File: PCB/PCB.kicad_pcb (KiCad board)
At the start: 2 copper layers, 0 parts

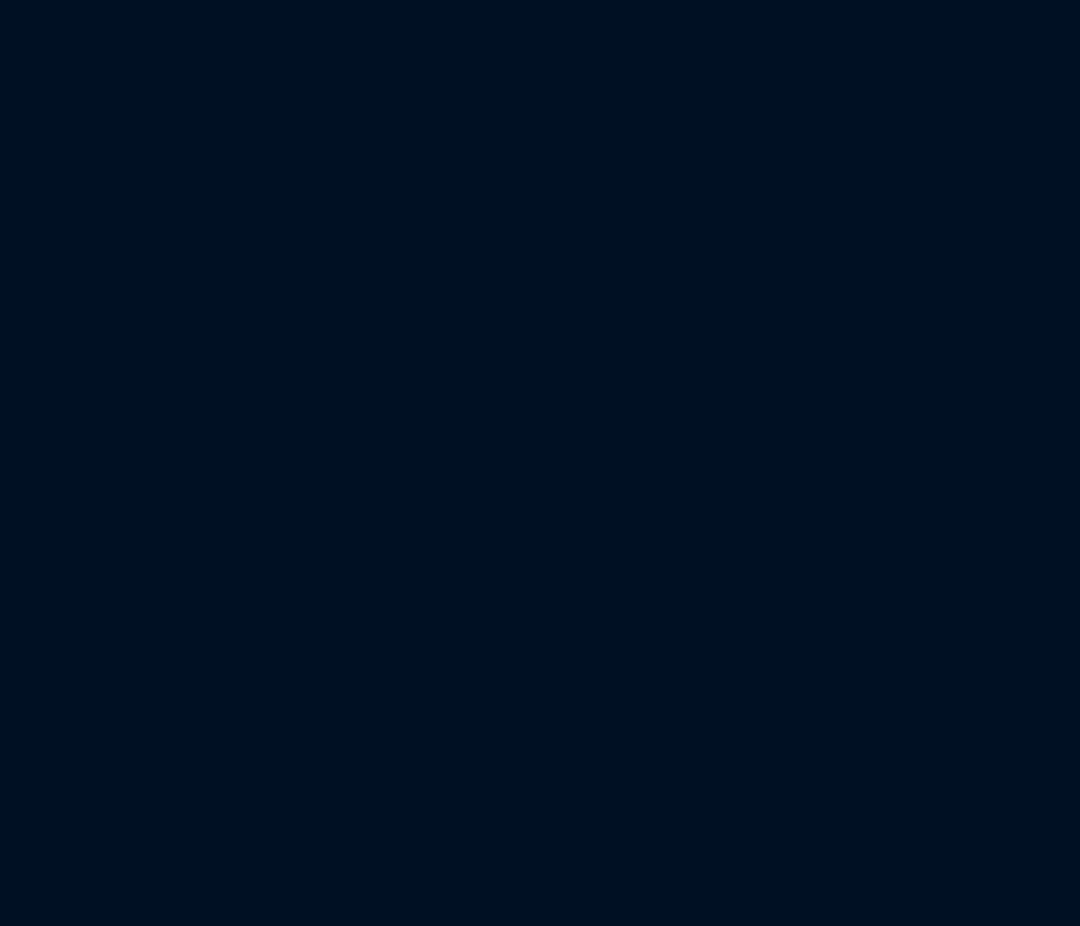
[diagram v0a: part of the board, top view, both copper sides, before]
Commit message: Confirm LCSC numbers
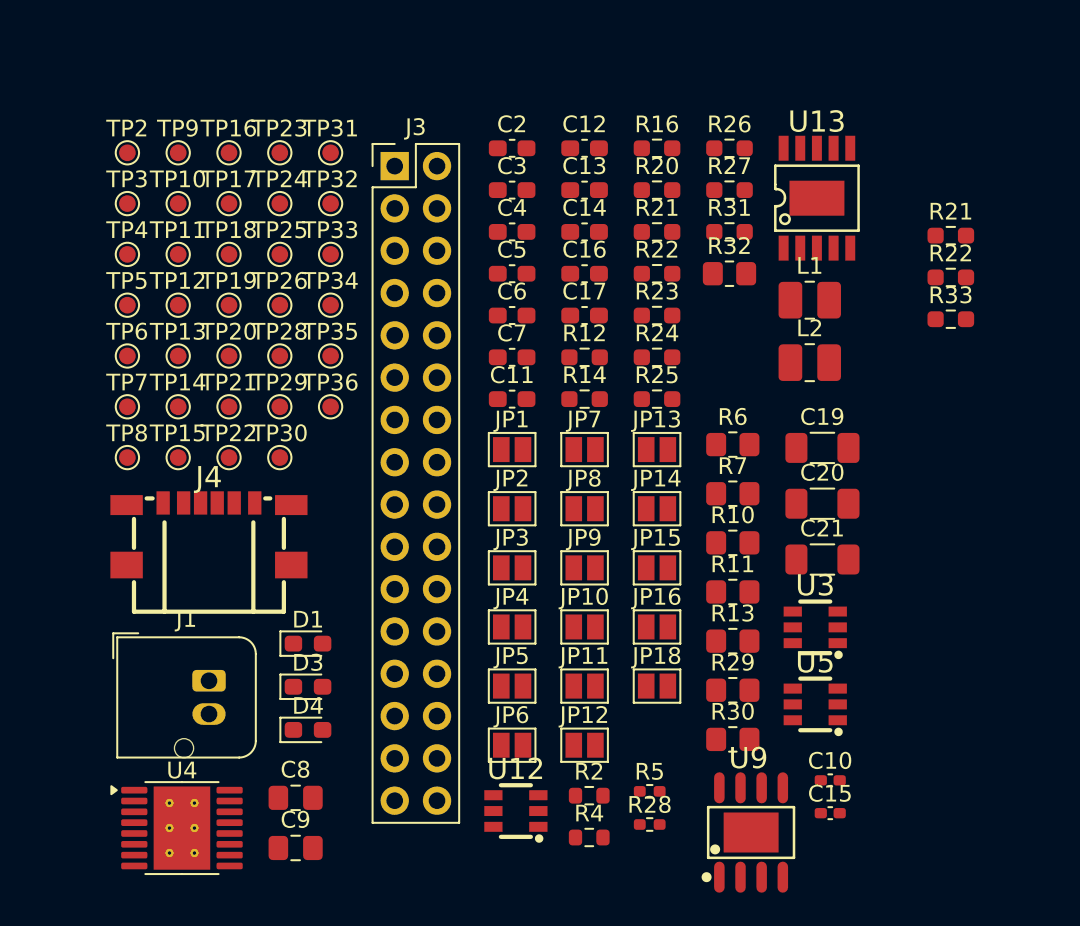
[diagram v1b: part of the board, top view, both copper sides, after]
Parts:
- added C10: 100n, Capacitor_SMD:C_0402_1005Metric_Pad0.74x0.62mm_HandSolder, F.Cu at (143.3, 109.7)
- added C11: 10u, Capacitor_SMD:C_0603_1608Metric_Pad1.08x0.95mm_HandSolder, F.Cu at (124.2, 86.8)
- added C12: 10u, Capacitor_SMD:C_0603_1608Metric_Pad1.08x0.95mm_HandSolder, F.Cu at (128.6, 71.7)
- added C13: 2.2u, Capacitor_SMD:C_0603_1608Metric_Pad1.08x0.95mm_HandSolder, F.Cu at (128.6, 74.2)
- added C14: 10u, Capacitor_SMD:C_0603_1608Metric_Pad1.08x0.95mm_HandSolder, F.Cu at (128.6, 76.8)
- added C15: 100n, Capacitor_SMD:C_0402_1005Metric_Pad0.74x0.62mm_HandSolder, F.Cu at (143.3, 111.7)
- added C16: 2.2u, Capacitor_SMD:C_0603_1608Metric_Pad1.08x0.95mm_HandSolder, F.Cu at (128.6, 79.3)
- added C17: 2.2u, Capacitor_SMD:C_0603_1608Metric_Pad1.08x0.95mm_HandSolder, F.Cu at (128.6, 81.8)
- added C19: 10u, Capacitor_SMD:C_1206_3216Metric_Pad1.33x1.80mm_HandSolder, F.Cu at (142.9, 89.7)
- added C2: 2.2u, Capacitor_SMD:C_0603_1608Metric_Pad1.08x0.95mm_HandSolder, F.Cu at (124.2, 71.7)
- added C20: 10u, Capacitor_SMD:C_1206_3216Metric_Pad1.33x1.80mm_HandSolder, F.Cu at (142.9, 93.1)
- added C21: 1u, Capacitor_SMD:C_1206_3216Metric_Pad1.33x1.80mm_HandSolder, F.Cu at (142.9, 96.4)
- added C3: 10u, Capacitor_SMD:C_0603_1608Metric_Pad1.08x0.95mm_HandSolder, F.Cu at (124.2, 74.2)
- added C4: 0.6u, Capacitor_SMD:C_0603_1608Metric_Pad1.08x0.95mm_HandSolder, F.Cu at (124.2, 76.8)
- added C5: 0.1u, Capacitor_SMD:C_0603_1608Metric_Pad1.08x0.95mm_HandSolder, F.Cu at (124.2, 79.3)
- added C6: 10u, Capacitor_SMD:C_0603_1608Metric_Pad1.08x0.95mm_HandSolder, F.Cu at (124.2, 81.8)
- added C7: 10u, Capacitor_SMD:C_0603_1608Metric_Pad1.08x0.95mm_HandSolder, F.Cu at (124.2, 84.3)
- added C8: 47u, Capacitor_SMD:C_0805_2012Metric_Pad1.18x1.45mm_HandSolder, F.Cu at (111.2, 110.7)
- added C9: 47u, Capacitor_SMD:C_0805_2012Metric_Pad1.18x1.45mm_HandSolder, F.Cu at (111.2, 113.7)
- added D1: LED, LED_SMD:LED_0603_1608Metric_Pad1.05x0.95mm_HandSolder, F.Cu at (112.0, 101.5)
- added D3: Red, LED_SMD:LED_0603_1608Metric_Pad1.05x0.95mm_HandSolder, F.Cu at (112.0, 104.1)
- added D4: LED, LED_SMD:LED_0603_1608Metric_Pad1.05x0.95mm_HandSolder, F.Cu at (112.0, 106.7)
- added J1: Conn_01x02_Pin, Connector_JST:JST_JWPF_B02B-JWPF-SK-R_1x02_P2.00mm_Vertical, F.Cu at (106.0, 103.7)
- added J3: Conn_02x16_Odd_Even, Connector_PinHeader_2.54mm:PinHeader_2x16_P2.54mm_Vertical, F.Cu at (117.2, 72.8)
- added J4: USB_C_Receptacle_PowerOnly_6P, Nhlamolo.:USB-C-SMD_TYPE-602-T3, F.Cu at (106.0, 94.9)
- added JP1: Jumper_2_Small_Open, Jumper:SolderJumper-2_P1.3mm_Open_Pad1.0x1.5mm, F.Cu at (124.2, 89.8)
- added JP10: Jumper_2_Small_Open, Jumper:SolderJumper-2_P1.3mm_Open_Pad1.0x1.5mm, F.Cu at (128.6, 100.5)
- added JP11: Jumper_2_Small_Open, Jumper:SolderJumper-2_P1.3mm_Open_Pad1.0x1.5mm, F.Cu at (128.6, 104.0)
- added JP12: Jumper_2_Small_Open, Jumper:SolderJumper-2_P1.3mm_Open_Pad1.0x1.5mm, F.Cu at (128.6, 107.6)
- added JP13: Jumper_2_Small_Open, Jumper:SolderJumper-2_P1.3mm_Open_Pad1.0x1.5mm, F.Cu at (132.9, 89.8)
- added JP14: Jumper_2_Small_Open, Jumper:SolderJumper-2_P1.3mm_Open_Pad1.0x1.5mm, F.Cu at (132.9, 93.4)
- added JP15: Jumper_2_Small_Open, Jumper:SolderJumper-2_P1.3mm_Open_Pad1.0x1.5mm, F.Cu at (132.9, 96.9)
- added JP16: Jumper_2_Small_Open, Jumper:SolderJumper-2_P1.3mm_Open_Pad1.0x1.5mm, F.Cu at (132.9, 100.5)
- added JP18: Jumper_2_Small_Open, Jumper:SolderJumper-2_P1.3mm_Open_Pad1.0x1.5mm, F.Cu at (132.9, 104.0)
- added JP2: Jumper_2_Small_Open, Jumper:SolderJumper-2_P1.3mm_Open_Pad1.0x1.5mm, F.Cu at (124.2, 93.4)
- added JP3: Jumper_2_Small_Open, Jumper:SolderJumper-2_P1.3mm_Open_Pad1.0x1.5mm, F.Cu at (124.2, 96.9)
- added JP4: Jumper_2_Small_Open, Jumper:SolderJumper-2_P1.3mm_Open_Pad1.0x1.5mm, F.Cu at (124.2, 100.5)
- added JP5: Jumper_2_Small_Open, Jumper:SolderJumper-2_P1.3mm_Open_Pad1.0x1.5mm, F.Cu at (124.2, 104.0)
- added JP6: Jumper_2_Small_Open, Jumper:SolderJumper-2_P1.3mm_Open_Pad1.0x1.5mm, F.Cu at (124.2, 107.6)
- added JP7: Jumper_2_Small_Open, Jumper:SolderJumper-2_P1.3mm_Open_Pad1.0x1.5mm, F.Cu at (128.6, 89.8)
- added JP8: Jumper_2_Small_Open, Jumper:SolderJumper-2_P1.3mm_Open_Pad1.0x1.5mm, F.Cu at (128.6, 93.4)
- added JP9: Jumper_2_Small_Open, Jumper:SolderJumper-2_P1.3mm_Open_Pad1.0x1.5mm, F.Cu at (128.6, 96.9)
- added L1: 2.2u, Inductor_SMD:L_1008_2520Metric_Pad1.43x2.20mm_HandSolder, F.Cu at (142.1, 80.9)
- added L2: 2.2u, Inductor_SMD:L_1008_2520Metric_Pad1.43x2.20mm_HandSolder, F.Cu at (142.1, 84.6)
- added R10: 200, Resistor_SMD:R_0805_2012Metric_Pad1.20x1.40mm_HandSolder, F.Cu at (137.5, 95.4)
- added R11: 200, Resistor_SMD:R_0805_2012Metric_Pad1.20x1.40mm_HandSolder, F.Cu at (137.5, 98.4)
- added R12: 0, Resistor_SMD:R_0603_1608Metric_Pad0.98x0.95mm_HandSolder, F.Cu at (128.6, 84.3)
- added R13: 5k6, Resistor_SMD:R_0805_2012Metric_Pad1.20x1.40mm_HandSolder, F.Cu at (137.5, 101.3)
- added R14: 1k, Resistor_SMD:R_0603_1608Metric_Pad0.98x0.95mm_HandSolder, F.Cu at (128.6, 86.8)
- added R16: 1k, Resistor_SMD:R_0603_1608Metric_Pad0.98x0.95mm_HandSolder, F.Cu at (132.9, 71.7)
- added R2: 1.8k, Resistor_SMD:R_0603_1608Metric, F.Cu at (128.9, 110.6)
- added R20: 0.2, Resistor_SMD:R_0603_1608Metric_Pad0.98x0.95mm_HandSolder, F.Cu at (132.9, 74.2)
- added R21: 200m, Resistor_SMD:R_0603_1608Metric_Pad0.98x0.95mm_HandSolder, F.Cu at (132.9, 76.8)
- added R21: 0.2, Resistor_SMD:R_0603_1608Metric_Pad0.98x0.95mm_HandSolder, F.Cu at (150.6, 77.0)
- added R22: 0.2, Resistor_SMD:R_0603_1608Metric_Pad0.98x0.95mm_HandSolder, F.Cu at (150.6, 79.5)
- added R22: 200m, Resistor_SMD:R_0603_1608Metric_Pad0.98x0.95mm_HandSolder, F.Cu at (132.9, 79.3)
- added R23: 200m, Resistor_SMD:R_0603_1608Metric_Pad0.98x0.95mm_HandSolder, F.Cu at (132.9, 81.8)
- added R24: 4.7k, Resistor_SMD:R_0603_1608Metric_Pad0.98x0.95mm_HandSolder, F.Cu at (132.9, 84.3)
- added R25: 1k8, Resistor_SMD:R_0603_1608Metric_Pad0.98x0.95mm_HandSolder, F.Cu at (132.9, 86.8)
- added R26: 0, Resistor_SMD:R_0603_1608Metric_Pad0.98x0.95mm_HandSolder, F.Cu at (137.3, 71.7)
- added R27: 4.7k, Resistor_SMD:R_0603_1608Metric_Pad0.98x0.95mm_HandSolder, F.Cu at (137.3, 74.2)
- added R28: 1k, Resistor_SMD:R_0402_1005Metric_Pad0.72x0.64mm_HandSolder, F.Cu at (132.5, 112.3)
- added R29: 6k8, Resistor_SMD:R_0805_2012Metric_Pad1.20x1.40mm_HandSolder, F.Cu at (137.5, 104.3)
- added R30: 10k, Resistor_SMD:R_0805_2012Metric_Pad1.20x1.40mm_HandSolder, F.Cu at (137.5, 107.2)
- added R31: 10k, Resistor_SMD:R_0603_1608Metric_Pad0.98x0.95mm_HandSolder, F.Cu at (137.3, 76.8)
- added R32: 10k, Resistor_SMD:R_0805_2012Metric_Pad1.20x1.40mm_HandSolder, F.Cu at (137.3, 79.3)
- added R33: 0.2, Resistor_SMD:R_0603_1608Metric_Pad0.98x0.95mm_HandSolder, F.Cu at (150.6, 82.0)
- added R4: 1.8k, Resistor_SMD:R_0603_1608Metric, F.Cu at (128.9, 113.1)
- added R5: 1k, Resistor_SMD:R_0402_1005Metric_Pad0.72x0.64mm_HandSolder, F.Cu at (132.5, 110.3)
- added R6: 10k, Resistor_SMD:R_0805_2012Metric_Pad1.20x1.40mm_HandSolder, F.Cu at (137.5, 89.5)
- added R7: 8.2k, Resistor_SMD:R_0805_2012Metric_Pad1.20x1.40mm_HandSolder, F.Cu at (137.5, 92.5)
- added TP10: TestPoint, TestPoint:TestPoint_Pad_D1.0mm, F.Cu at (104.2, 75.1)
- added TP11: TestPoint, TestPoint:TestPoint_Pad_D1.0mm, F.Cu at (104.2, 78.1)
- added TP12: TestPoint, TestPoint:TestPoint_Pad_D1.0mm, F.Cu at (104.2, 81.2)
- added TP13: TestPoint, TestPoint:TestPoint_Pad_D1.0mm, F.Cu at (104.2, 84.2)
- added TP14: TestPoint, TestPoint:TestPoint_Pad_D1.0mm, F.Cu at (104.2, 87.3)
- added TP15: TestPoint, TestPoint:TestPoint_Pad_D1.0mm, F.Cu at (104.2, 90.3)
- added TP16: TestPoint, TestPoint:TestPoint_Pad_D1.0mm, F.Cu at (107.2, 72.0)
- added TP17: TestPoint, TestPoint:TestPoint_Pad_D1.0mm, F.Cu at (107.2, 75.1)
- added TP18: TestPoint, TestPoint:TestPoint_Pad_D1.0mm, F.Cu at (107.2, 78.1)
- added TP19: TestPoint, TestPoint:TestPoint_Pad_D1.0mm, F.Cu at (107.2, 81.2)
- added TP2: TestPoint, TestPoint:TestPoint_Pad_D1.0mm, F.Cu at (101.1, 72.0)
- added TP20: TestPoint, TestPoint:TestPoint_Pad_D1.0mm, F.Cu at (107.2, 84.2)
- added TP21: TestPoint, TestPoint:TestPoint_Pad_D1.0mm, F.Cu at (107.2, 87.3)
- added TP22: TestPoint, TestPoint:TestPoint_Pad_D1.0mm, F.Cu at (107.2, 90.3)
- added TP23: TestPoint, TestPoint:TestPoint_Pad_D1.0mm, F.Cu at (110.3, 72.0)
- added TP24: TestPoint, TestPoint:TestPoint_Pad_D1.0mm, F.Cu at (110.3, 75.1)
- added TP25: TestPoint, TestPoint:TestPoint_Pad_D1.0mm, F.Cu at (110.3, 78.1)
- added TP26: TestPoint, TestPoint:TestPoint_Pad_D1.0mm, F.Cu at (110.3, 81.2)
- added TP28: TestPoint, TestPoint:TestPoint_Pad_D1.0mm, F.Cu at (110.3, 84.2)
- added TP29: TestPoint, TestPoint:TestPoint_Pad_D1.0mm, F.Cu at (110.3, 87.3)
- added TP3: TestPoint, TestPoint:TestPoint_Pad_D1.0mm, F.Cu at (101.1, 75.1)
- added TP30: TestPoint, TestPoint:TestPoint_Pad_D1.0mm, F.Cu at (110.3, 90.3)
- added TP31: TestPoint, TestPoint:TestPoint_Pad_D1.0mm, F.Cu at (113.3, 72.0)
- added TP32: TestPoint, TestPoint:TestPoint_Pad_D1.0mm, F.Cu at (113.3, 75.1)
- added TP33: TestPoint, TestPoint:TestPoint_Pad_D1.0mm, F.Cu at (113.3, 78.1)
- added TP34: TestPoint, TestPoint:TestPoint_Pad_D1.0mm, F.Cu at (113.3, 81.2)
- added TP35: TestPoint, TestPoint:TestPoint_Pad_D1.0mm, F.Cu at (113.3, 84.2)
- added TP36: TestPoint, TestPoint:TestPoint_Pad_D1.0mm, F.Cu at (113.3, 87.3)
- added TP4: TestPoint, TestPoint:TestPoint_Pad_D1.0mm, F.Cu at (101.1, 78.1)
- added TP5: TestPoint, TestPoint:TestPoint_Pad_D1.0mm, F.Cu at (101.1, 81.2)
- added TP6: TestPoint, TestPoint:TestPoint_Pad_D1.0mm, F.Cu at (101.1, 84.2)
- added TP7: TestPoint, TestPoint:TestPoint_Pad_D1.0mm, F.Cu at (101.1, 87.3)
- added TP8: TestPoint, TestPoint:TestPoint_Pad_D1.0mm, F.Cu at (101.1, 90.3)
- added TP9: TestPoint, TestPoint:TestPoint_Pad_D1.0mm, F.Cu at (104.2, 72.0)
- added U12: TS5A3159ADBVR, Nhlamolo.:SOT-23-6_L2.9-W1.6-P0.95-LS2.8-BR, F.Cu at (124.5, 111.5)
- added U13: CH224K, Nhlamolo.:ESSOP-10_L4.9-W3.9-P1.0-LS6.0-TL-EP, F.Cu at (142.5, 74.7)
- added U3: TPS22917DBV, Nhlamolo.:SOT-23-6_L2.9-W1.6-P0.95-LS2.8-BR, F.Cu at (142.4, 100.5)
- added U4: DRV8833PWP, Package_SO:HTSSOP-16-1EP_4.4x5mm_P0.65mm_EP3.4x5mm_Mask2.46x2.31mm_ThermalVias, F.Cu at (104.4, 112.6)
- added U5: TPS22917DBV, Nhlamolo.:SOT-23-6_L2.9-W1.6-P0.95-LS2.8-BR, F.Cu at (142.4, 105.1)
- added U9: TP4056-42-ESOP8, Nhlamolo.:ESOP-8_L4.9-W3.9-P1.27-LS6.0-BL-EP-1, F.Cu at (138.6, 112.8)

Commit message: Before PCB layout
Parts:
- removed C20: 10u, Capacitor_SMD:C_1206_3216Metric_Pad1.33x1.80mm_HandSolder
- removed JP12, JP13: Jumper_2_Small_Open, Jumper:SolderJumper-2_P1.3mm_Open_Pad1.0x1.5mm
- removed R20, R21, R22, R33: 0.2, Resistor_SMD:R_0603_1608Metric_Pad0.98x0.95mm_HandSolder
- removed R21, R22, R23: 200m, Resistor_SMD:R_0603_1608Metric_Pad0.98x0.95mm_HandSolder
- removed R26: 0, Resistor_SMD:R_0603_1608Metric_Pad0.98x0.95mm_HandSolder
- removed TP15, TP16, TP17, TP18, TP28, TP29, TP31, TP5: TestPoint, TestPoint:TestPoint_Pad_D1.0mm
- removed U12: TS5A3159ADBVR, Nhlamolo.:SOT-23-6_L2.9-W1.6-P0.95-LS2.8-BR
- removed U13: CH224K, Nhlamolo.:ESSOP-10_L4.9-W3.9-P1.0-LS6.0-TL-EP
- removed U3, U5: TPS22917DBV, Nhlamolo.:SOT-23-6_L2.9-W1.6-P0.95-LS2.8-BR
- removed U9: TP4056-42-ESOP8, Nhlamolo.:ESOP-8_L4.9-W3.9-P1.27-LS6.0-BL-EP-1
- added C22: 10u, Capacitor_SMD:C_0603_1608Metric_Pad1.08x0.95mm_HandSolder, F.Cu at (272.2, 136.0)
- added JP17: Jumper_2_Small_Open, Jumper:SolderJumper-2_P1.3mm_Open_Pad1.0x1.5mm, F.Cu at (272.2, 83.3)
- added JP19: Jumper_2_Small_Open, Jumper:SolderJumper-2_P1.3mm_Open_Pad1.0x1.5mm, F.Cu at (272.2, 90.5)
- added JP21: Jumper_2_Small_Open, Jumper:SolderJumper-2_P1.3mm_Open_Pad1.0x1.5mm, F.Cu at (272.2, 94.0)
- added JP22: Jumper_2_Small_Open, Jumper:SolderJumper-2_P1.3mm_Open_Pad1.0x1.5mm, F.Cu at (272.2, 97.5)
- added JP23: Jumper_2_Small_Open, Jumper:SolderJumper-2_P1.3mm_Open_Pad1.0x1.5mm, F.Cu at (272.2, 101.1)
- added JP24: Jumper_2_Small_Open, Jumper:SolderJumper-2_P1.3mm_Open_Pad1.0x1.5mm, F.Cu at (272.2, 104.7)
- added R15: 0.22, Library:R2512, F.Cu at (247.3, 100.6)
- added R17: 0.22, Library:R2512, F.Cu at (247.3, 105.7)
- added R18: 0.22, Library:R2512, F.Cu at (247.3, 110.7)
- added R19: 0.22, Library:R2512, F.Cu at (247.3, 115.8)
- added R8: 0.22, Library:R2512, F.Cu at (247.3, 85.4)
- added R9: 0.22, Library:R2512, F.Cu at (247.3, 90.5)
- added SW1: SW_Nidec_CAS-120A1, Library:SW-TH_1MS1T1B1M1QES-5, F.Cu at (249.6, 138.7)
- added TP27: TestPoint, TestPoint:TestPoint_Pad_D1.0mm, F.Cu at (272.0, 114.0)
- added TP37: TestPoint, TestPoint:TestPoint_THTPad_D2.5mm_Drill1.2mm, F.Cu at (205.3, 107.4)
- added TP38: TestPoint, TestPoint:TestPoint_THTPad_D2.5mm_Drill1.2mm, F.Cu at (205.3, 112.0)
- added TP39: TestPoint, TestPoint:TestPoint_Pad_D1.0mm, F.Cu at (275.1, 117.1)
- added TP40: TestPoint, TestPoint:TestPoint_Pad_D1.0mm, F.Cu at (275.1, 120.2)
- added U1: DRV8833PWPR, Library:DRV8833PWPR, F.Cu at (212.5, 108.2)
- added U10: TPS63020, Library:TPS63020DSJR, F.Cu at (99.8, 178.8)
- added U11: TPS63020, Library:TPS63020DSJR, F.Cu at (159.5, 187.5)
- added U2: INA219AxDCN, Library:INA219AIDCNR, F.Cu at (210.0, 113.4)
- C10, C15: footprint Capacitor_SMD:C_0402_1005Metric_Pad0.74x0.62mm_HandSolder -> Capacitor_SMD:C_0603_1608Metric_Pad1.08x0.95mm_HandSolder
- C19, C21: footprint Capacitor_SMD:C_1206_3216Metric_Pad1.33x1.80mm_HandSolder -> Capacitor_SMD:C_0603_1608Metric_Pad1.08x0.95mm_HandSolder
- C4: value 0.6u -> 1u
- J4: footprint Nhlamolo.:USB-C-SMD_TYPE-602-T3 -> Connector_USB:USB_C_Receptacle_GCT_USB4110
- R12: value 0 -> 0.22; footprint Resistor_SMD:R_0603_1608Metric_Pad0.98x0.95mm_HandSolder -> Library:R2512
- R28, R5: footprint Resistor_SMD:R_0402_1005Metric_Pad0.72x0.64mm_HandSolder -> Resistor_SMD:R_0603_1608Metric_Pad0.98x0.95mm_HandSolder
- R31: footprint Resistor_SMD:R_0603_1608Metric_Pad0.98x0.95mm_HandSolder -> Resistor_SMD:R_0805_2012Metric_Pad1.20x1.40mm_HandSolder
- moved TP23 165.8 mm to (268.9, 120.2)
- moved TP24 165.8 mm to (268.9, 123.2)
- moved TP2 165.6 mm to (262.9, 108.0)
- moved TP3 165.6 mm to (262.9, 111.0)
- moved TP4 165.6 mm to (262.9, 114.0)
- moved TP10 165.6 mm to (265.9, 111.0)
- moved TP11 165.6 mm to (265.9, 114.0)
- moved TP12 165.6 mm to (265.9, 117.1)
- moved TP13 165.6 mm to (265.9, 120.2)
- moved TP14 165.6 mm to (265.9, 123.2)
- moved TP9 165.6 mm to (265.9, 108.0)
- moved TP6 165.0 mm to (262.9, 117.1)
- moved TP7 165.0 mm to (262.9, 120.2)
- moved TP8 165.0 mm to (262.9, 123.2)
- moved TP32 164.9 mm to (272.0, 120.2)
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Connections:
- C4 pad 1: Net-(U2-IN+) -> Battery
- C4 pad 2: Net-(U2-IN-) -> Load_Supply
- J1 pad 1: unconnected-(J1-Pin_1-Pad1) -> Net-(J1-Pin_1)
- J4 pad A9: /HV_Pin -> High_Voltage_(9V)
- J4 pad B9: /HV_Pin -> High_Voltage_(9V)
- JP16 pad 1: /5V_PG -> Load_Supply
- JP16 pad 2: 5V Out -> Net-(JP16-B)
- R12 pad 1: Battery -> GND
- R12 pad 2: Net-(U2-IN+) -> Net-(JP1-B)
- R28 pad 1: /HV_Pin -> High_Voltage_(9V)
- R31 pad 2: /5V_Out -> Net-(JP17-B)
- R6 pad 1: /HV-Pin -> High_Voltage_(9V)
- TP19 pad 1: Load_Supply -> /3V3_Out
- TP2 pad 1: Battery -> Net-(JP19-B)
- TP20 pad 1: Battery -> MOTOR3_A_OUT
- TP22 pad 1: I2C1_SDA -> MOTOR4_A_OUT
- TP23 pad 1: I2C1_SCL -> /M4AB2
- TP26 pad 1: MOTOR1_B_OUT -> /M3AO2
- TP3 pad 1: /HV_Pin -> High_Voltage_(9V)
- TP30 pad 1: MOTOR1_B_OUT -> /M2BO2
- TP32 pad 1: MOTOR1_B_OUT -> MOTOR2_A_OUT
- TP33 pad 1: /5V_Out -> Net-(JP17-B)
- TP36 pad 1: Net-(JP18-A) -> MOTOR1_A_OUT
- U4 pad 4: MOTOR3_B_OUT -> /M3AO2
- U4 pad 5: MOTOR4_B_OUT -> /M4AB2

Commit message: Begining of PCB Layout
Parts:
- added JP13: Jumper_3_Open, Jumper:SolderJumper-3_P1.3mm_Open_Pad1.0x1.5mm, F.Cu at (132.7, 107.5)
- moved R14 250.3 mm to (27.1, 147.0)
- moved C16 245.4 mm to (27.1, 139.0)
- moved JP24 242.6 mm to (29.6, 106.0)
- moved JP21 241.7 mm to (30.6, 102.0)
- moved TP7 240.9 mm to (22.0, 116.0)
- moved C3 240.6 mm to (23.1, 140.0)
- moved TP9 238.9 mm to (27.4, 121.0)
- moved C17 238.3 mm to (34.1, 140.0)
- moved C2 238.0 mm to (26.1, 143.0)
- moved C13 237.0 mm to (31.1, 146.0)
- moved JP23 235.6 mm to (36.6, 103.0)
- moved JP22 234.8 mm to (37.6, 109.0)
- moved TP12 233.3 mm to (33.0, 130.0)
- moved TP6 232.9 mm to (30.0, 116.0)
- moved TP30 229.2 mm to (46.0, 155.0)
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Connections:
- U1 pad 3: /AISEN1 -> GND
- U1 pad 6: /BISEN1 -> GND
- U4 pad 3: /AISEN2 -> GND
- U4 pad 6: /BISEN2 -> GND
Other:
- board outline added: 161.4 x 161.4 mm
